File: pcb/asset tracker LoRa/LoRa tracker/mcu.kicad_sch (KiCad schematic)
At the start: 5 parts, among them CON2 jtag, U7 ATSAMD21

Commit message: pcb kastje
pcb in kastje getekend
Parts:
- removed C20: 10uF, vanalles:0603, symbol Device:C_Small
- removed U7: ATSAMD21, halfgeleiders:QFN49P40_600X600X90L40X20T460N, symbol Halfgelijders:ATSAMD21
- added C33, C34: 20pF, vanalles:0603, symbol Device:C_Small
- added U7: ATSAMD21G18A-M, halfgeleiders:QFN50P700X700X90-49N, symbol MCU_Microchip_SAMD:ATSAMD21G18A-M
- added Y2: Crystal, vanalles:crystal tht, symbol Device:Crystal
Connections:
- net +3V3: now also U7.17 (VDDIO), U7.36 (VDDIO), U7.43 (VDDCORE), U7.44 (VDDIN), U7.6 (VDDANA)
- net BUZZER_OUT_MCU: now also U7.27 (PA18)
- net CS_RFM: now also U7.23 (PA14)
- net GND: now also CON2.9 (GND), C33.1, C34.1, U7.18 (GND), U7.35 (GND), U7.42 (GND), U7.5 (GNDANA)
- net GPS_PPS_MCU: now also U7.29 (PA20)
- net GPS_RESET_MCU: now also U7.31 (PA22)
- net GPS_WAKE_MCU: now also U7.30 (PA21)
- net LIS_INT1_MCU: now also U7.25 (PA16)
- net LIS_INT2_MCU: now also U7.26 (PA17)
- net RST: now also U7.40 (~RESET)
- net RX_MCU: now also U7.10 (PA05)
- net SCL_MCU: now also U7.33 (PA24)
- net SCR_OUT_MCU: now also U7.28 (PA19)
- net SDA_MCU: now also U7.32 (PA23)
- net SWDCLK: now also U7.45 (PA30)
- net SWDIO: now also U7.46 (PA31)
- net TX_MCU: now also U7.11 (PA06)
- new net: C33.2, U7.1 (PA00), Y2.2
- new net: C34.2, U7.2 (PA01), Y2.1
- new net MISO_MURATTA_MCU: U7.24 (PA15)
- new net MOSI_MURATTA_MCU: U7.21 (PA12)
- new net RESET_MURATTA_MCU: U7.39 (PA27)
- new net SCK_MURATTA_MCU: U7.22 (PA13)
- no-connect marks 19 -> 13

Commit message: lora tracker
lora tracker afgemaakt
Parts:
- U7: footprint halfgeleiders:QFN50P700X700X90-49N -> halfgeleiders:ATSAMD21G18A-M
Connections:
- net GND: now also U7.49 (EP)
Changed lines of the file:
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@@
   (junction (at 100.33 52.07) (diameter 0.9144) (color 0 0 0 0))
   (junction (at 140.97 134.62) (diameter 0.9144) (color 0 0 0 0))
+  (junction (at 142.24 134.62) (diameter 0.9144) (color 0 0 0 0))
   (junction (at 147.32 38.1) (diameter 0.9144) (color 0 0 0 0))
   (junction (at 167.64 29.21) (diameter 0.9144) (color 0 0 0 0))
@@
     (stroke (width 0) (type solid) (color 0 0 0 0))
   )
+  (wire (pts (xy 142.24 134.62) (xy 147.32 134.62))
+    (stroke (width 0) (type solid) (color 0 0 0 0))
+  )
   (wire (pts (xy 147.32 38.1) (xy 167.64 38.1))
     (stroke (width 0) (type solid) (color 0 0 0 0))
@@
     (property "Reference" "U7" (id 0) (at 140.97 118.11 0))
     (property "Value" "ATSAMD21G18A-M" (id 1) (at 140.97 120.65 0))
-    (property "Footprint" "halfgeleiders:QFN50P700X700X90-49N" (id 2) (at 175.26 133.35 0)
-      (effects (font (size 1.27 1.27)) hide)
-    )
+    (property "Footprint" "halfgeleiders:ATSAMD21G18A-M" (id 2) (at 175.26 133.35 0)
+      (effects (font (size 1.27 1.27)) hide)
+    )

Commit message: klaar
print hertekend naar stm32L5
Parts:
- removed C21: 10uF, vanalles:0603, symbol Device:C_Small
- removed C22: 100nF, vanalles:0603, symbol Device:C_Small
- removed C33, C34: 20pF, vanalles:0603, symbol Device:C_Small
- removed U7: ATSAMD21G18A-M, halfgeleiders:ATSAMD21G18A-M, symbol MCU_Microchip_SAMD:ATSAMD21G18A-M
- added BT2: Battery_Cell, vanalles:3012TR, symbol Device:Battery_Cell
- added C20: 100nF, vanalles:0603, symbol vanalles:capacitor
- added C21: 1uF, vanalles:0603, symbol vanalles:capacitor
- added C22, C33: 6.8pF, vanalles:0603, symbol vanalles:capacitor
- added R11: R_Small_US, vanalles:0603RL, symbol Device:R_Small_US
- added U7: STM32L552CCT6, halfgeleiders:STM32L552CCT6, symbol 2021-05-31_10-35-08:STM32L552CCT6
- added Y3: 16MHz, vanalles:MURATA_CSTCE16M0V53C-R0, symbol Device:Resonator
- Y2: value Crystal -> 32khz
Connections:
- net +3V3: now also C20.1, C21.1, U7.24 (VDD), U7.36 (VDD), U7.48 (VDD), U7.7 (NRST), U7.9 (VDDA/VREF+)
- net BUZZER_OUT_MCU: now also U7.31 (PA10)
- net CS_RFM: now also U7.14 (PA4)
- net GND: now also BT2.2 (-), C20.2, C21.2, C22.2, C33.2, R11.2, U7.23 (VSS), U7.35 (VSS), U7.47 (VSS), U7.8 (VSSA/VREF-), Y3.2
- net GPS_PPS_MCU: now also U7.26 (PB13)
- net GPS_RESET_MCU: now also U7.28 (PB15)
- net GPS_WAKE_MCU: now also U7.27 (PB14)
- net LIS_INT1_MCU: now also U7.33 (PA12)
- net LIS_INT2_MCU: now also U7.32 (PA11)
- net MISO_MURATTA_MCU: now also U7.16 (PA6)
- net MOSI_MURATTA_MCU: now also U7.17 (PA7)
- net RESET_MURATTA_MCU: now also U7.29 (PA8)
- net RST: now also U7.40 (PB4NJTRST)
- net RX_MCU: now also U7.11 (PA1)
- net SCK_MURATTA_MCU: now also U7.15 (PA5)
- net SCL_MCU: now also U7.42 (PB6)
- net SCR_OUT_MCU: now also U7.30 (PA9)
- net SDA_MCU: now also U7.43 (PB7)
- net SWDCLK: now also U7.37 (PA14JTCK/SWCLK)
- net SWDIO: now also U7.34 (PA13JTMS/SWDIO)
- net TX_MCU: now also U7.10 (PA0)
- net OSC_32_IN: now reaches Y2.2
- net OSC_32_IN: now also C22.1, U7.3 (PC14-OSC32_INPC14)
- net OSC_32_OUT: now reaches Y2.1
- net OSC_32_OUT: now also C33.1, U7.4 (PC15-OSC32_OUTPC15)
- net SWO: now reaches CON2.6 (SWO/TDO)
- net SWO: now also U7.39 (PB3JTDO/TRACESWO)
- net TDI: now reaches CON2.8 (NC/TDI)
- net TDI: now also U7.38 (PA15JTDI)
- new net: R11.1, U7.44 (PH3-BOOT0)
- new net: BT2.1 (+), U7.1 (VBAT)
- new net OSC_HS_IN: U7.5 (PH0-OSC_INPH0), Y3.3
- new net OSC_HS_OUT: U7.6 (PH1-OSC_OUTPH1), Y3.1
- no-connect marks 13 -> 12

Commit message: verandering
iets veranderd
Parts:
- R11: value R_Small_US -> 10K
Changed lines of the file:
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@@
       (effects (font (size 1.27 1.27)) (justify left))
     )
-    (property "Value" "R_Small_US" (id 1) (at 270.51 86.9949 0)
+    (property "Value" "10K" (id 1) (at 270.51 86.9949 0)
       (effects (font (size 1.27 1.27)) (justify left))
     )

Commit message: code
code
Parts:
- Y3: footprint vanalles:MURATA_CSTCE16M0V53C-R0 -> vanalles:MURATA_CSTLS16M0X53-B0
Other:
- moved on the sheet: CON2, R11, U7A

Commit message: schema
schema hergetekend
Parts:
- removed BT2: Battery_Cell, vanalles:3012TR, symbol Device:Battery_Cell
- removed R11: 10K, vanalles:0603RL, symbol Device:R_Small_US
- removed U7: STM32L552CCT6, halfgeleiders:STM32L552CCT6, symbol 2021-05-31_10-35-08:STM32L552CCT6
- removed Y3: 16MHz, vanalles:MURATA_CSTLS16M0X53-B0, symbol Device:Resonator
- added U7: STM32L052K6Tx, halfgeleiders:QFP32P80_900X900X160L60X37N, symbol MCU_ST_STM32L0:STM32L052K6Tx
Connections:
- net +3V3: now also U7.1 (VDD), U7.17 (VDD), U7.5 (VDDA)
- net BUZZER_OUT_MCU: now also U7.6 (PA0)
- net GND: now also U7.16 (VSS), U7.31 (BOOT0), U7.32 (VSS)
- net GPS_PPS_MCU: now also U7.22 (PA12)
- net GPS_RESET_MCU: now also U7.18 (PA8)
- net GPS_WAKE_MCU: now also U7.21 (PA11)
- net LIS_INT1_MCU: now also U7.28 (PB5)
- net LIS_INT2_MCU: now also U7.27 (PB4)
- net MISO_MURATTA_MCU: now also U7.12 (PA6)
- net MOSI_MURATTA_MCU: now also U7.13 (PA7)
- net OSC_32_IN: now also U7.2 (PC14)
- net OSC_32_OUT: now also U7.3 (PC15)
- net RESET_MURATTA_MCU: now also U7.9 (PA3)
- net RST: now also U7.4 (NRST)
- net RX_MCU: now also U7.20 (PA10)
- net SCK_MURATTA_MCU: now also U7.11 (PA5)
- net SCL_MCU: now also U7.29 (PB6)
- net SCR_OUT_MCU: now also U7.7 (PA1)
- net SDA_MCU: now also U7.30 (PB7)
- net SWDCLK: now also U7.24 (PA14)
- net SWDIO: now also U7.23 (PA13)
- net TX_MCU: now also U7.19 (PA9)
- net SWO: no longer names the net of CON2.6 (SWO/TDO)
- net TDI: no longer names the net of CON2.8 (NC/TDI)
- new net CS_MURATTA_MCU: U7.10 (PA4)
- no-connect marks 12 -> 8
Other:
- moved on the sheet: C20, C21

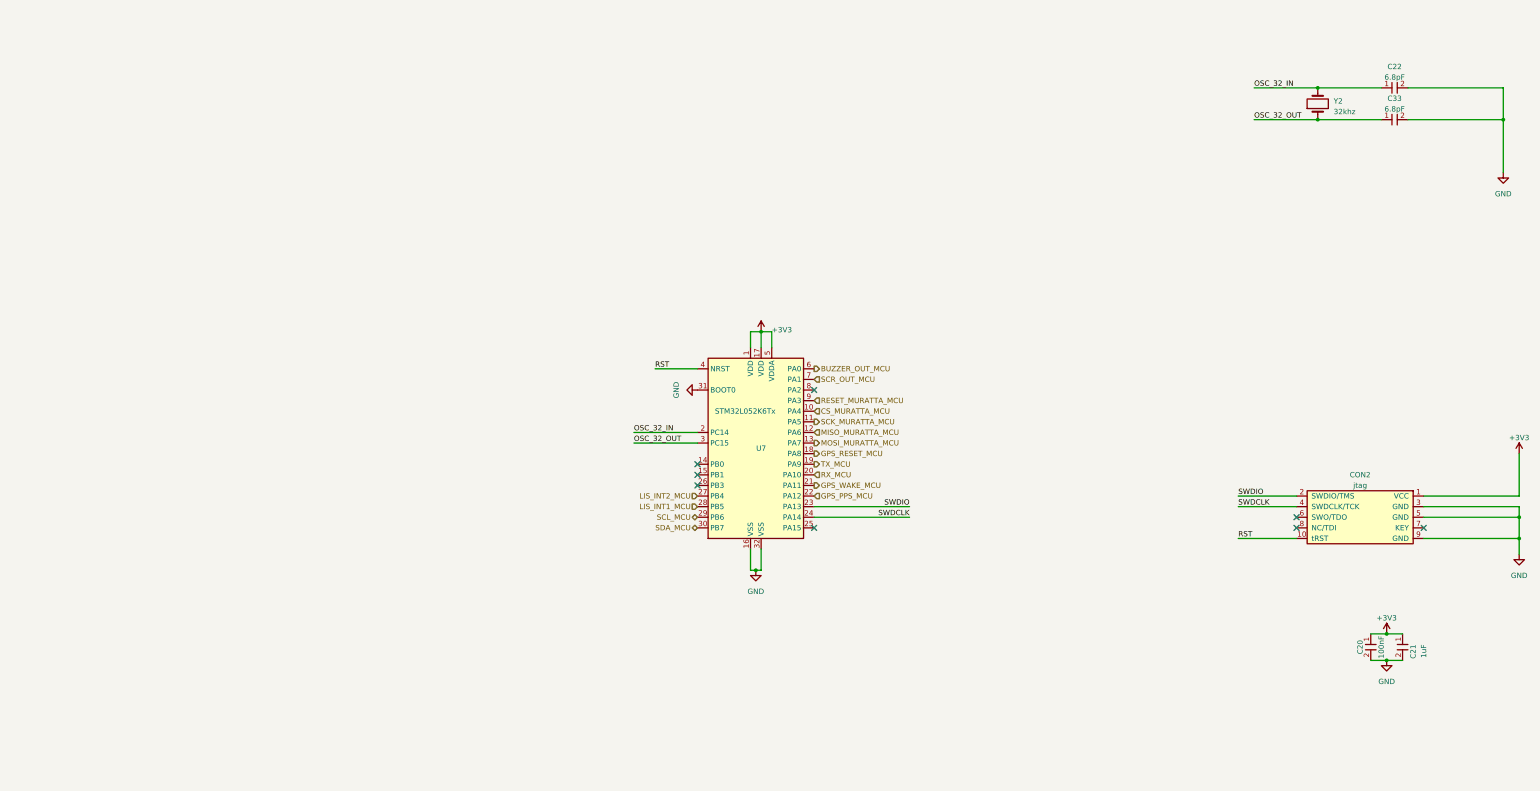
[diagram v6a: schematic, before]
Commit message: versie2
aan versie 2 begonnen met tekenen en code beginnen schrijven voor quadkey
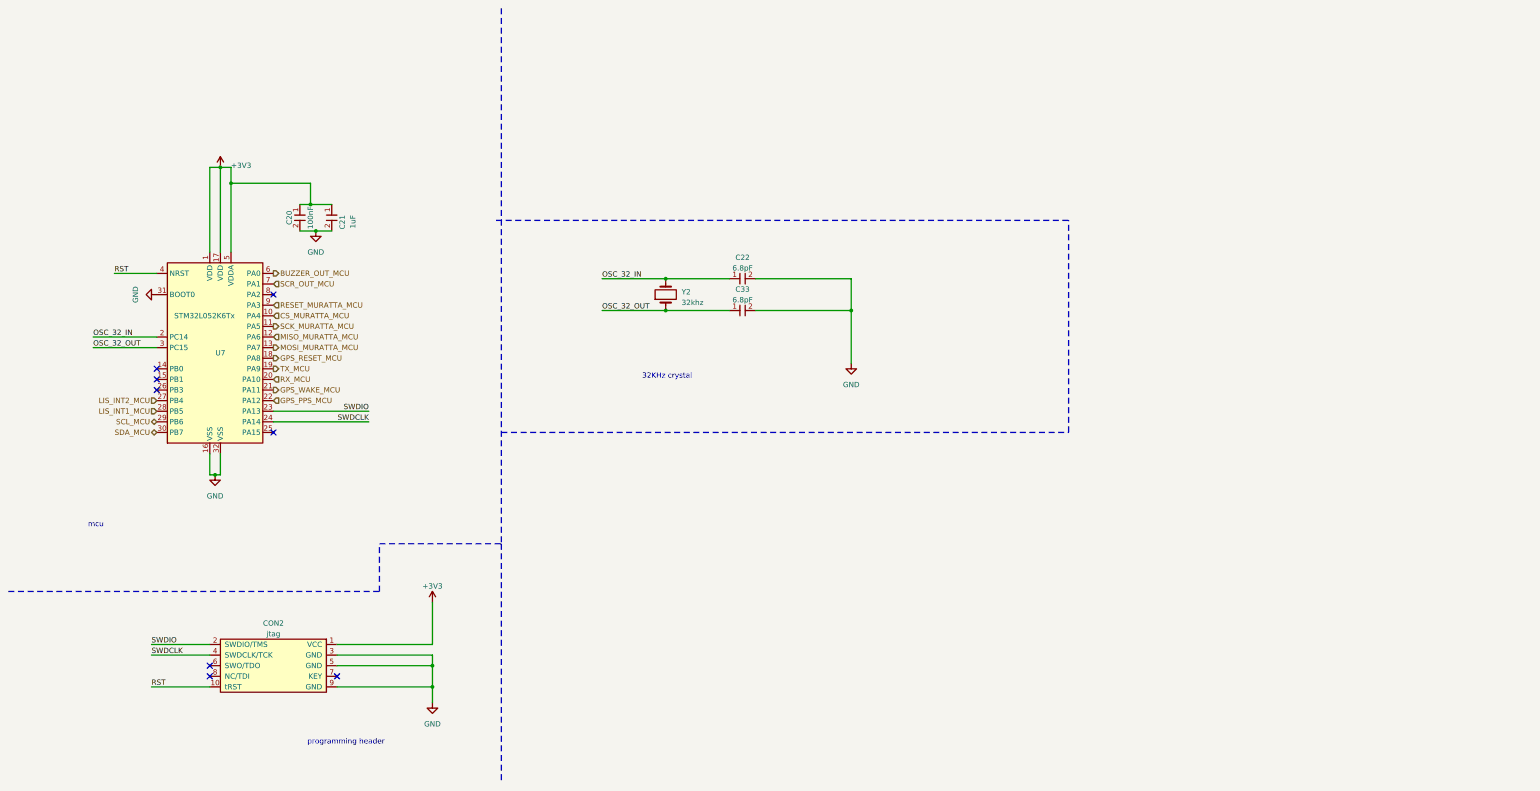
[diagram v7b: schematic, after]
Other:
- note added: "32KHz crystal"
- note added: "mcu"
- note added: "programming header"
- moved on the sheet: C20, C21, C22, C33, CON2, U7, Y2
